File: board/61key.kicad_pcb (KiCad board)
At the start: 2 copper layers, 295.3 x 104.8 mm, 144 parts, among them J1 105450-0101, SW1 SW_SPST, SW10 SW_SPST, SW11 SW_SPST, SW12 SW_SPST, SW13 SW_SPST, SW14 SW_SPST, SW15 SW_SPST, SW16 SW_SPST, SW17 SW_SPST, SW18 SW_SPST, SW19 SW_SPST, SW2 SW_SPST, SW20 SW_SPST, SW21 SW_SPST, SW22 SW_SPST, SW23 SW_SPST, SW24 SW_SPST, SW25 SW_SPST, SW26 SW_SPST, SW27 SW_SPST, SW28 SW_SPST, SW29 SW_SPST, SW3 SW_SPST, SW30 SW_SPST, SW31 SW_SPST, SW32 SW_SPST, SW33 SW_SPST, SW34 SW_SPST, SW35 SW_SPST, SW36 SW_SPST, SW37 SW_SPST, SW38 SW_SPST, SW39 SW_SPST, SW4 SW_SPST, SW40 SW_SPST, SW41 SW_SPST, SW42 SW_SPST, SW43 SW_SPST, SW44 SW_SPST, SW45 SW_SPST, SW46 SW_SPST, SW47 SW_SPST, SW48 SW_SPST, SW49 SW_SPST, SW5 SW_SPST, SW50 SW_SPST, SW51 SW_SPST, SW52 SW_SPST, SW53 SW_SPST, SW54 SW_SPST, SW55 SW_SPST, SW56 SW_SPST, SW57 SW_SPST, SW58 SW_SPST, SW59 SW_SPST, SW6 SW_SPST, SW60 SW_SPST, SW61 SW_SPST, SW7 SW_SPST, SW8 SW_SPST, SW9 SW_SPST, U1 ATmega32U4-AU, X1 FA-238

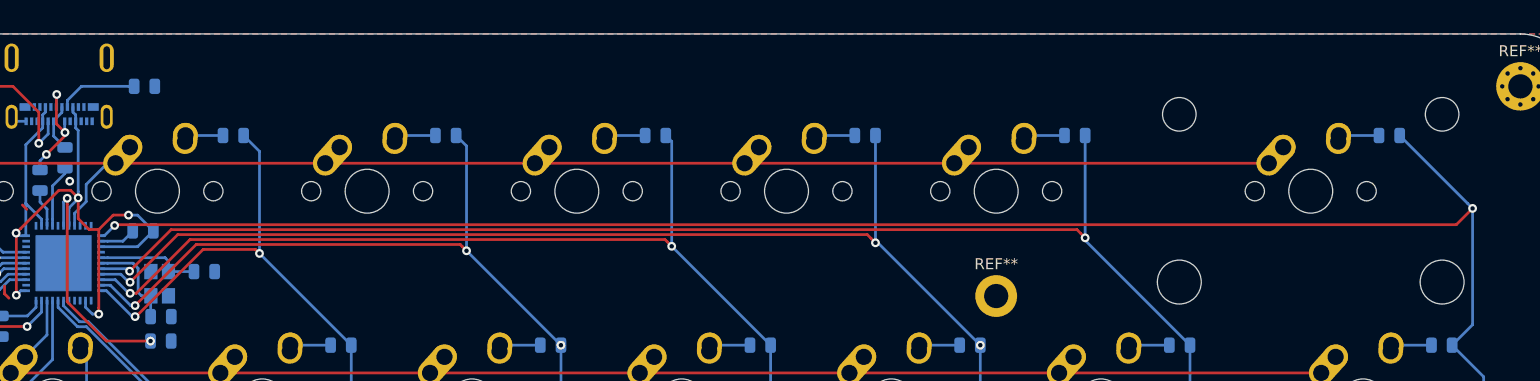
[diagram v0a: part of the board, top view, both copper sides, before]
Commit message: add pads, new step
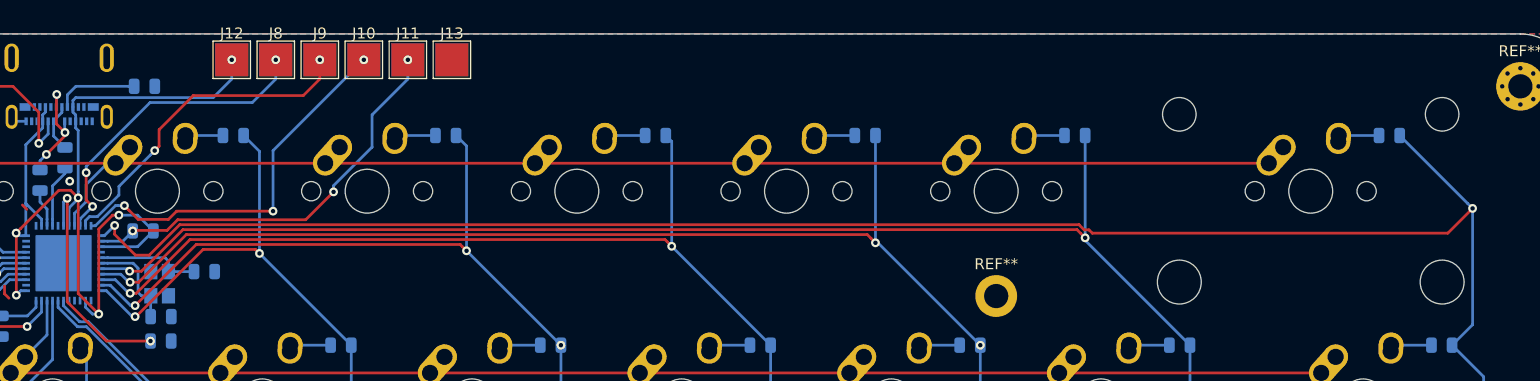
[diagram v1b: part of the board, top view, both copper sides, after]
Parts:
- added J10: Conn_01x01_Male, TestPoint:TestPoint_Pad_3.0x3.0mm, F.Cu at (209.2, 59.5)
- added J11: Conn_01x01_Male, TestPoint:TestPoint_Pad_3.0x3.0mm, F.Cu at (213.2, 59.5)
- added J12: Conn_01x01_Male, TestPoint:TestPoint_Pad_3.0x3.0mm, F.Cu at (197.2, 59.5)
- added J13: Conn_01x01_Male, TestPoint:TestPoint_Pad_3.0x3.0mm, F.Cu at (217.2, 59.5)
- added J2: Conn_01x01_Male, TestPoint:TestPoint_Pad_3.0x3.0mm, B.Cu at (201.2, 59.5)
- added J3: Conn_01x01_Male, TestPoint:TestPoint_Pad_3.0x3.0mm, B.Cu at (205.2, 59.5)
- added J4: Conn_01x01_Male, TestPoint:TestPoint_Pad_3.0x3.0mm, B.Cu at (209.2, 59.5)
- added J5: Conn_01x01_Male, TestPoint:TestPoint_Pad_3.0x3.0mm, B.Cu at (213.2, 59.5)
- added J6: Conn_01x01_Male, TestPoint:TestPoint_Pad_3.0x3.0mm, B.Cu at (197.2, 59.5)
- added J7: Conn_01x01_Male, TestPoint:TestPoint_Pad_3.0x3.0mm, B.Cu at (217.2, 59.5)
- added J8: Conn_01x01_Male, TestPoint:TestPoint_Pad_3.0x3.0mm, F.Cu at (201.2, 59.5)
- added J9: Conn_01x01_Male, TestPoint:TestPoint_Pad_3.0x3.0mm, F.Cu at (205.2, 59.5)
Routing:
- net /MISO: track 0.00 -> 35.3 mm, vias 0 -> 3
- net /RESET: track 3.29 -> 37.8 mm, vias 0 -> 3
- net /MOSI: track 0.00 -> 30.2 mm, vias 0 -> 2
- net /SCLK: track 0.00 -> 28.4 mm, vias 0 -> 3
- net VCC: track 67.0 -> 91.8 mm, vias 5 -> 6
- net /col13: track 206.7 -> 210.1 mm

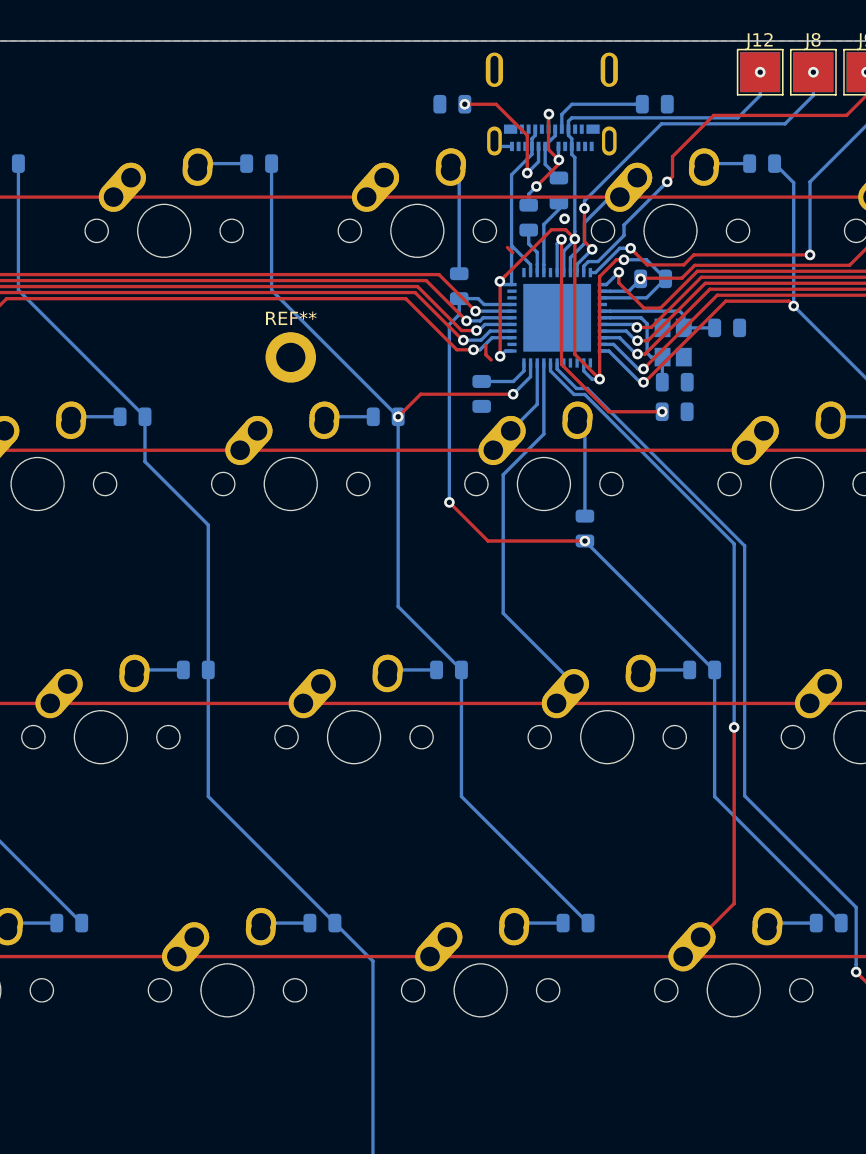
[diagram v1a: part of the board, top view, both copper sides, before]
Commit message: add better img and logo
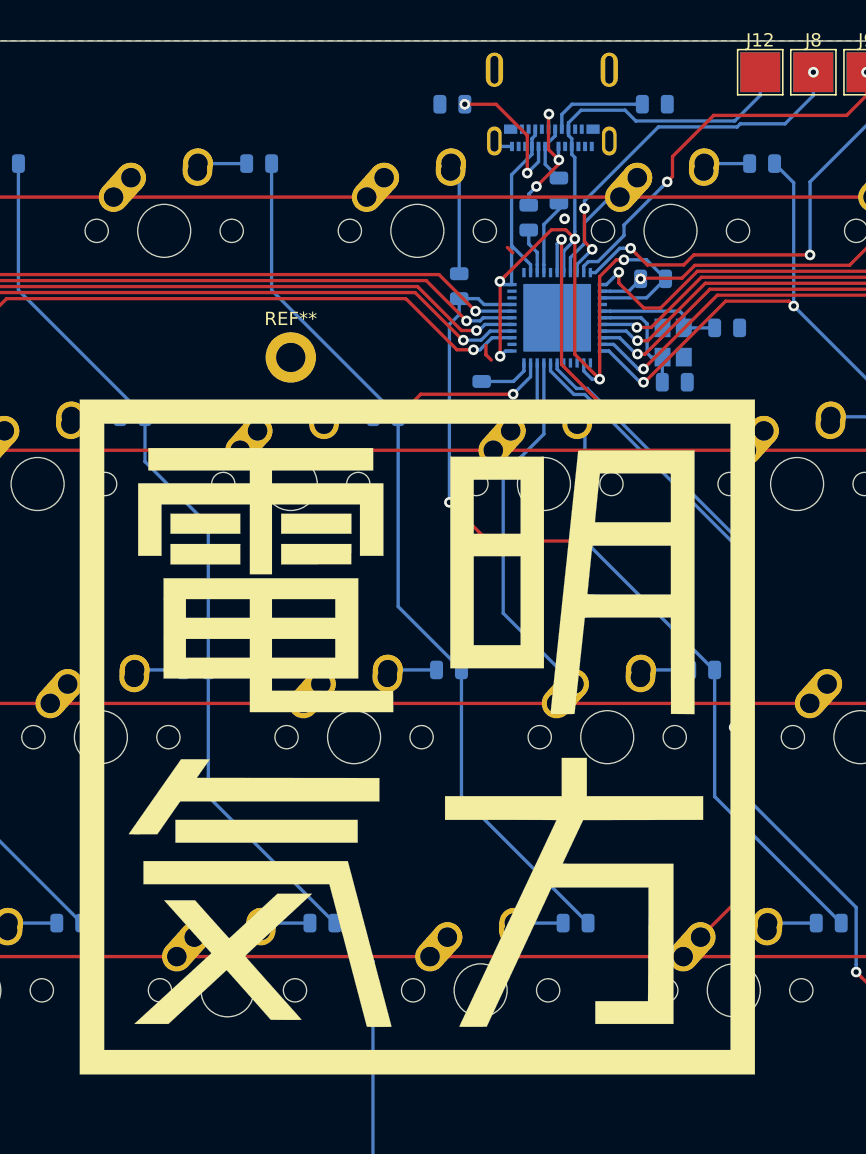
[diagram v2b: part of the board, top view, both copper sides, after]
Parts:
- added G***: LOGO, 61key:logo, F.Cu at (171.4, 109.5)
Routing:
- net VCC: track 91.8 -> 92.4 mm, vias 6 -> 5

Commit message: new images, backplate, clean up for smt assembly
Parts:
- removed the REF** at (161.9, 81.0)
- removed the REF** at (100.0, 119.1)
- removed the REF** at (181.0, 147.6)
- added C4: C, Capacitor_SMD:C_0805_2012Metric, B.Cu at (193.8, 74.6)
- added REF**: MountingHole_2.2mm_M2_DIN965_Pad, MountingHole:MountingHole_2.2mm_M2_DIN965_Pad, F.Cu at (171.4, 61.9)
- added REF**: MountingHole_2.2mm_M2_DIN965_Pad, MountingHole:MountingHole_2.2mm_M2_DIN965_Pad, F.Cu at (171.4, 97.6)
- added REF**: MountingHole_2.2mm_M2_DIN965_Pad, MountingHole:MountingHole_2.2mm_M2_DIN965_Pad, F.Cu at (76.2, 119.1)
- added REF**: MountingHole_2.2mm_M2_DIN965_Pad, MountingHole:MountingHole_2.2mm_M2_DIN965_Pad, F.Cu at (171.4, 147.6)
- D1, D10, D11, D12, D13, D14, D15, D16, D17, D18, D19, D2, D20, D21, D22, D23, D24, D25, D26, D27, D28, D29, D3, D30, D31, D32, D33, D34, D35, D36, D37, D38, D39, D4, D40, D41, D42, D43, D44, D45, D46, D47, D48, D49, D5, D50, D51, D52, D53, D54, D55, D56, D57, D58, D59, D6, D60, D61, D7, D8, D9: footprint Diode_SMD:D_0805_2012Metric -> 61key:D_0805_2012Metric
- J10, J11, J12, J13, J2, J3, J4, J5, J6, J7, J8, J9: footprint TestPoint:TestPoint_Pad_3.0x3.0mm -> 61key:pad-nosilk
- moved REF** 23.8 mm to (266.7, 119.1)
- moved R1 6.62 mm to (176.7, 68.0), turned to 270 degrees
- moved C2 0.35 mm to (190.8, 85.4)
- moved C1 0.24 mm to (190.8, 83.1)
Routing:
- net Net-(J1-PadA5): track 10.9 -> 5.42 mm
- net /col6: track 79.3 -> 82.0 mm
- net Net-(J1-PadA7): track 10.3 -> 11.3 mm
- net VCC: track 92.4 -> 93.1 mm, vias 5 -> 6
- net Net-(J1-PadB5): track 7.49 -> 8.05 mm
- net /RESET: track 37.8 -> 38.2 mm, vias 3 -> 4
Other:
- board text added: "GND"
- board text added: "J1"
- board text added: "MISO"
- board text added: "MOSI"
- board text added: "RESET"
- board text added: "SCLK"
- board text added: "VCC"

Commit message: big overhaul
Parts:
- removed C1, C2, C3, C4: C, Capacitor_SMD:C_0805_2012Metric
- removed D56: D, 61key:D_0805_2012Metric
- removed J1: 105450-0101, 61key:MOLEX_105450-0101
- removed J10, J11, J12, J13, J2, J3, J4, J5, J6, J7, J8, J9: Conn_01x01_Male, 61key:pad-nosilk
- removed R1, R3, R4, R5, R6: R_US, Resistor_SMD:R_0805_2012Metric
- removed REF** (x7): MountingHole_2.2mm_M2_DIN965_Pad, MountingHole:MountingHole_2.2mm_M2_DIN965_Pad
- removed REF** (x4): MountingHole_2.2mm_M2_Pad_Via, MountingHole:MountingHole_2.2mm_M2_Pad_Via
- removed U1: ATmega32U4-AU, 61key:QFN-44-1EP_7x7mm_Pitch0.5mm
- removed X1: FA-238, 61key:OSCCC320X250X70-4N
- added D62: D, 61key:D_0805_2012Metric, B.Cu at (311.9, 66.4)
- added D63: D, 61key:D_0805_2012Metric, B.Cu at (69.1, 123.5)
- added D64: D, 61key:D_0805_2012Metric, B.Cu at (295.3, 123.8)
- added D65: D, 61key:D_0805_2012Metric, B.Cu at (311.9, 123.8)
- added SW62: SW_SPST, 61key:SW_MX, F.Cu at (304.8, 71.4)
- added SW63: SW_SPST, 61key:SW_MX, F.Cu at (285.8, 71.4)
- added SW64: SW_SPST, 61key:SW_MX, F.Cu at (40.5, 128.6)
- added SW65: SW_SPST, 61key:SW_MX, F.Cu at (61.9, 128.6)
- added SW66: SW_SPST, 61key:SW_MX, F.Cu at (259.6, 128.6)
- added SW67: SW_SPST, 61key:SW_MX, F.Cu at (285.8, 128.6)
- added SW68: SW_SPST, 61key:SW_MX, F.Cu at (304.8, 128.6)
- SW1, SW11, SW12, SW13, SW14, SW16, SW17, SW18, SW19, SW21, SW22, SW23, SW24, SW26, SW27, SW28, SW29, SW31, SW32, SW33, SW34, SW36, SW37, SW38, SW39, SW41, SW42, SW43, SW44, SW45, SW46, SW47, SW48, SW49, SW50, SW51, SW52, SW53, SW54, SW55, SW57, SW58, SW6, SW7, SW8, SW9: footprint 61key:MX-1U-NoLED -> 61key:SW_MX
- SW10, SW15, SW25, SW30, SW35, SW40, SW5: footprint 61key:MX-1.25U-NoLED -> 61key:SW_MX
- SW2, SW61: footprint 61key:MX-1.5U-NoLED -> 61key:SW_MX
- SW20: footprint 61key:MX-6.25U-NoLED -> 61key:SW_MX
- SW3: footprint 61key:MX-1.75U-NoLED -> 61key:SW_MX
- SW4, SW59: footprint 61key:MX-2.25U-NoLED -> 61key:SW_MX
- SW56: footprint 61key:MX-2.75U-NoLED -> 61key:SW_MX
- SW60: footprint 61key:MX-2U-NoLED -> 61key:SW_MX
- moved D59 15.6 mm to (302.4, 104.8), turned to 180 degrees
- moved D9 14.1 mm to (87.8, 123.5), turned to 180 degrees
- moved D36 10.1 mm to (178.6, 66.4), turned to 180 degrees
- moved D4 9.53 mm to (47.6, 123.5)
- moved D37 9.34 mm to (188.1, 85.4), turned to 180 degrees
- moved D8 8.33 mm to (70.2, 104.5), turned to 0 degrees
- moved D12 8.33 mm to (84.5, 85.4), turned to 0 degrees
- moved D7 8.04 mm to (65.8, 85.4), turned to 0 degrees
- moved D13 8.04 mm to (89.6, 104.5), turned to 0 degrees
- moved D15 6.53 mm to (90.5, 138.1), turned to 90 degrees
- moved D52 4.47 mm to (259.6, 119.1)
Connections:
- net /row3 renamed Net-(SW14-Pad1)
- D10 pad 1: /col1 -> Net-(D10-Pad1)
- D14 pad 1: /col2 -> /col3
- D15 pad 1: /col2 -> Net-(D15-Pad1)
- D19 pad 1: /col3 -> /col4
- D20 pad 1: /col5 -> Net-(D20-Pad1)
- D24 pad 1: /col4 -> /col5
- D25 pad 1: /col9 -> Net-(D25-Pad1)
- D29 pad 1: /col5 -> /col6
- D30 pad 1: /col10 -> Net-(D30-Pad1)
- D34 pad 1: /col6 -> /col7
- D35 pad 1: /col11 -> Net-(D35-Pad1)
- D39 pad 1: /col7 -> /col8
- D40 pad 1: /col13 -> /col14
- D44 pad 1: /col8 -> /col9
- D48 pad 1: /col9 -> /col10
- D5 pad 1: /col0 -> Net-(D5-Pad1)
- D52 pad 1: /col10 -> /col11
- D59 pad 1: /col12 -> /col13
- D9 pad 1: /col1 -> /col2
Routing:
- net /col0: track 222.1 -> 0.00 mm, vias 2 -> 0
- net /col13: track 210.1 -> 0.00 mm, vias 2 -> 0
- net /col1: track 194.5 -> 0.00 mm, vias 2 -> 0
- net /col2: track 181.4 -> 0.00 mm, vias 2 -> 0
- net /col11: track 161.8 -> 0.00 mm, vias 3 -> 0
- net /col10: track 141.7 -> 0.00 mm, vias 2 -> 0
- net /col3: track 138.4 -> 0.00 mm, vias 2 -> 0
- net /col12: track 132.6 -> 0.00 mm, vias 2 -> 0
- net /col9: track 123.6 -> 0.00 mm, vias 3 -> 0
- net /col4: track 119.6 -> 0.00 mm, vias 2 -> 0
- net VCC: track 93.1 -> 0.00 mm, vias 6 -> 0
- net /col5: track 87.5 -> 0.00 mm
- net /col8: track 85.1 -> 0.00 mm, vias 2 -> 0
- net /col6: track 82.0 -> 0.00 mm, vias 2 -> 0
- net /row4: track 348.0 -> 266.8 mm, vias 1 -> 0
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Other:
- board text added: "ISO <>\"
- board text added: "ISO shift"
- board text added: "arrow key layout /?"
- board text added: "arrow key up arrow"
- board text added: "esc"
- board text added: "normal backspace"
- board text added: "split backspace"
- board text added: "standard 2.75u shift"
- board text added: "standard shift"

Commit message: layouts done, need to add traces
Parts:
- removed G***: LOGO, 61key:logo
- added >NAME: >VALUE, 61key:MX_STAB_6.75U, F.Cu at (159.5, 147.6)
- added >NAME: >VALUE, 61key:MX_STAB_2.75U, F.Cu at (288.1, 128.6)
- added >NAME: >VALUE, 61key:MX_STAB_2.25U, F.Cu at (50.0, 128.6)
- added >NAME: >VALUE, 61key:MX_STAB_2.25U, F.Cu at (292.9, 109.5)
- added D56: D, 61key:D_0805_2012Metric, B.Cu at (311.9, 142.9)
- added ST72: Stabilizer, 61key:MX_STAB_2U, F.Cu at (302.4, 100.0)
- added ST72: Stabilizer, 61key:MX_STAB_2U, F.Cu at (295.3, 71.4)
- added SW69: SW_SPST, 61key:SW_MX, F.Cu at (228.6, 147.6)
- added SW70: SW_SPST, 61key:SW_MX, F.Cu at (247.7, 147.6)
- added SW71: SW_SPST, 61key:SW_MX, F.Cu at (266.7, 147.6)
- added SW72: SW_SPST, 61key:SW_MX, F.Cu at (285.8, 147.6)
- added SW73: SW_SPST, 61key:SW_MX, F.Cu at (304.8, 147.6)
- added SW74: SW_SPST, 61key:SW_MX, F.Cu at (281.0, 109.5)
- added SW75: SW_SPST, 61key:SW_MX, F.Cu at (302.4, 100.0)
- moved D40 13.5 mm to (296.2, 140.5)
- moved D35 9.75 mm to (276.2, 140.5)
- moved D30 7.44 mm to (254.8, 140.5)
- moved D59 3.40 mm to (299.0, 104.7)
- moved D25 0.48 mm to (237.6, 142.6)
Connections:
- D35 pad 1: Net-(D35-Pad1) -> /col11
- D40 pad 1: /col14 -> /col13
- SW40 pad 2: Net-(D40-Pad2) -> Net-(D56-Pad2)
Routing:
- net /row1: track 257.2 -> 271.9 mm
- net Net-(D59-Pad2): track 0.00 -> 11.9 mm
- net Net-(D35-Pad2): track 0.00 -> 11.9 mm
- net Net-(D30-Pad2): track 0.00 -> 7.14 mm
- net Net-(D25-Pad2): track 0.00 -> 5.58 mm
- net Net-(D4-Pad2): track 5.87 -> 10.5 mm
- net /row4: track 266.8 -> 269.1 mm
- net Net-(D56-Pad2): track 0.00 -> 2.38 mm
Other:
- board text added: "ANSI backspace"
- board text added: "ANSI enter"
- board text added: "ANSI mod keys"
- board text added: "ANSI shift"
- board text added: "ISO enter"
- board text added: "ISO layout \|"
- board text added: "arrow key layout mod keys"
- board text added: "arrow key layout shift"
- board text added: "standard /?"
- board text removed: "GND"
- board text removed: "MISO"
- board text removed: "MOSI"
- board text removed: "RESET"
- board text removed: "SCLK"
- board text removed: "VCC"
- board text removed: "normal backspace"
- board text removed: "standard 2.75u shift"

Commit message: rows and columns for all layouts done
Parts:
- moved D25 16.3 mm to (221.5, 140.5), turned to 0 degrees
- moved D37 14.4 mm to (173.8, 83.3), turned to 0 degrees
- moved D55 14.4 mm to (254.8, 102.4), turned to 0 degrees
- moved D54 14.4 mm to (250.0, 83.3), turned to 0 degrees
- moved D51 14.4 mm to (235.7, 102.4), turned to 0 degrees
- moved D50 14.4 mm to (231.0, 83.3), turned to 0 degrees
- moved D47 14.4 mm to (216.7, 102.4), turned to 0 degrees
- moved D46 14.4 mm to (211.9, 83.3), turned to 0 degrees
- moved D43 14.4 mm to (197.6, 102.4), turned to 0 degrees
- moved D42 14.4 mm to (192.9, 83.3), turned to 0 degrees
- moved D38 14.4 mm to (178.6, 102.4), turned to 0 degrees
- moved D20 14.4 mm to (152.4, 140.5), turned to 0 degrees
- moved D33 14.4 mm to (159.5, 102.4), turned to 0 degrees
- moved D32 14.4 mm to (154.8, 83.3), turned to 0 degrees
- moved D28 14.4 mm to (140.5, 102.4), turned to 0 degrees
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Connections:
- D10 pad 1: Net-(D10-Pad1) -> /col1
- D15 pad 1: Net-(D15-Pad1) -> /col2
- D20 pad 1: Net-(D20-Pad1) -> /col6
- D25 pad 1: Net-(D25-Pad1) -> /col9
- D30 pad 1: Net-(D30-Pad1) -> /col10
- D5 pad 1: Net-(D5-Pad1) -> /col0
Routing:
- net /col13: track 0.00 -> 92.2 mm
- net /col11: track 0.00 -> 91.1 mm
- net /col6: track 0.00 -> 85.4 mm
- net /col0: track 0.00 -> 85.1 mm
- net /col2: track 0.00 -> 84.9 mm
- net /col10: track 0.00 -> 84.7 mm
- net /col1: track 0.00 -> 84.7 mm
- net /col9: track 0.00 -> 84.4 mm
- net /col14: track 0.00 -> 76.5 mm
- net /col5: track 0.00 -> 63.5 mm
- net /col4: track 0.00 -> 63.5 mm
- net /col8: track 0.00 -> 63.4 mm
- net /col3: track 0.00 -> 63.4 mm
- net /col7: track 0.00 -> 63.2 mm
- net /col12: track 0.00 -> 19.6 mm
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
